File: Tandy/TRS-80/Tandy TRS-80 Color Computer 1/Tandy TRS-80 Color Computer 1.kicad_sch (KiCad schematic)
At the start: 254 parts, among them K1 R7336-1, P1 CARTRIDGE CONNECTOR, P2 DIN-4, P3 DIN-6, P4 DIN-6, P5 DIN-5, Q1 MPS3904, Q2 2N6594, Q3 TIP29, T1 TRANSFORMER, U1 MC6809E, U10 MC6883, U11 74LS138, U12 MC1372, U13 723C, U14 LM339, U15 741C, U16 74LS244, U17 78M12, U18 79M12, U19 79L05, U2 MC14050B, U20 MCM4027A, U21 MCM4027A, U22 MCM4027A, U23 MCM4027A, U24 MCM4027A, U25 MCM4027A, U26 MCM4027A, U27 MCM4027A, U28 MCM68A364, U29 74LS02, U3 MCM68A364, U4 MC6821, U5 UM1285-8 RF Modulator, U6 74LS273, U7 MC6847, U8 MC6821, U9 MC14529B, X1 14.31818MHz

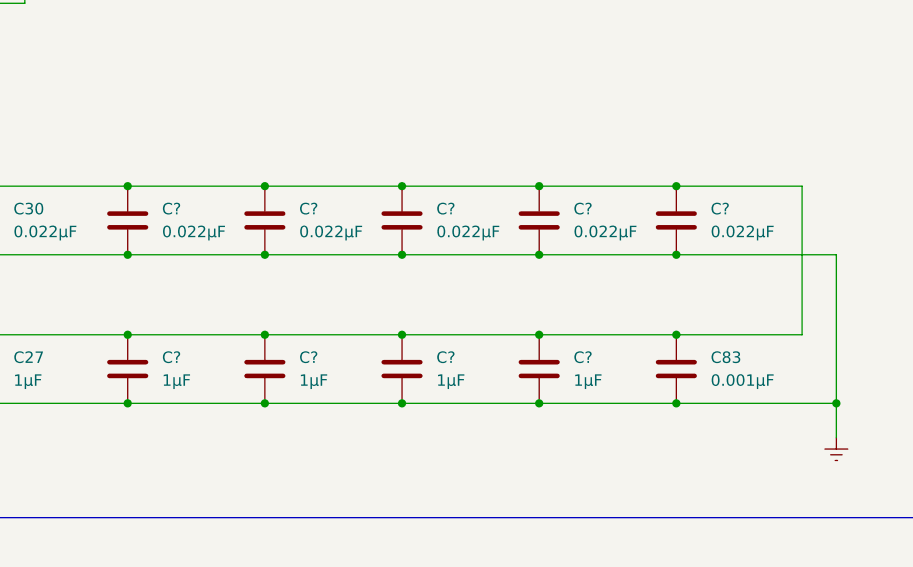
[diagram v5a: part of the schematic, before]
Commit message: Forgot to annotate some caps, fixed!
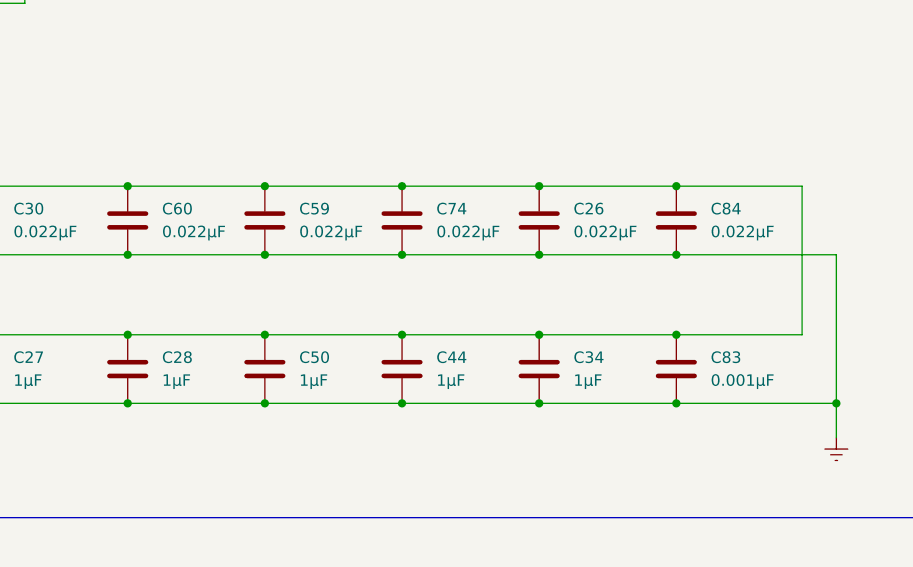
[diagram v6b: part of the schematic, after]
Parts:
- gave numbers to parts that had none: 9
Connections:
- net at E2.: now also T1.; no longer S2.
- net at S2.: now also E1.; no longer CR11. (-)
- net at E1.: now also T1.; no longer S2.
- new net: E2., S2.
- new net: CR11. (-), S2.
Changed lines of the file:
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@@
   (symbol (lib_id "Device:C") (at 646.43 887.73 0) (mirror y) (unit 1)
     (in_bom yes) (on_board yes) (fields_autoplaced)
-    (property "Reference" "C?" (id 0) (at 650.24 886.4599 0)
+    (property "Reference" "C28" (id 0) (at 650.24 886.4599 0)
       (effects (font (size 1.27 1.27)) (justify right))
     )
@@
   (symbol (lib_id "Device:C") (at 661.67 887.73 0) (mirror y) (unit 1)
     (in_bom yes) (on_board yes) (fields_autoplaced)
-    (property "Reference" "C?" (id 0) (at 665.48 886.4599 0)
+    (property "Reference" "C50" (id 0) (at 665.48 886.4599 0)
       (effects (font (size 1.27 1.27)) (justify right))
     )
@@
   (symbol (lib_id "Device:C") (at 646.43 871.22 0) (mirror y) (unit 1)
     (in_bom yes) (on_board yes) (fields_autoplaced)
-    (property "Reference" "C?" (id 0) (at 650.24 869.9499 0)
+    (property "Reference" "C60" (id 0) (at 650.24 869.9499 0)
       (effects (font (size 1.27 1.27)) (justify right))
     )
@@
   (symbol (lib_id "Device:C") (at 692.15 887.73 0) (mirror y) (unit 1)
     (in_bom yes) (on_board yes) (fields_autoplaced)
-    (property "Reference" "C?" (id 0) (at 695.96 886.4599 0)
+    (property "Reference" "C34" (id 0) (at 695.96 886.4599 0)
       (effects (font (size 1.27 1.27)) (justify right))
     )
@@
   (symbol (lib_id "Device:C") (at 676.91 871.22 0) (mirror y) (unit 1)
     (in_bom yes) (on_board yes) (fields_autoplaced)
-    (property "Reference" "C?" (id 0) (at 680.72 869.9499 0)
+    (property "Reference" "C74" (id 0) (at 680.72 869.9499 0)
       (effects (font (size 1.27 1.27)) (justify right))
     )
@@
   (symbol (lib_id "Device:C") (at 707.39 871.22 0) (mirror y) (unit 1)
     (in_bom yes) (on_board yes) (fields_autoplaced)
-    (property "Reference" "C?" (id 0) (at 711.2 869.9499 0)
+    (property "Reference" "C84" (id 0) (at 711.2 869.9499 0)
       (effects (font (size 1.27 1.27)) (justify right))
     )
@@
   (symbol (lib_id "Device:C") (at 676.91 887.73 0) (mirror y) (unit 1)
     (in_bom yes) (on_board yes) (fields_autoplaced)
-    (property "Reference" "C?" (id 0) (at 680.72 886.4599 0)
+    (property "Reference" "C44" (id 0) (at 680.72 886.4599 0)
       (effects (font (size 1.27 1.27)) (justify right))
     )
@@
   (symbol (lib_id "Device:C") (at 692.15 871.22 0) (mirror y) (unit 1)
     (in_bom yes) (on_board yes) (fields_autoplaced)
-    (property "Reference" "C?" (id 0) (at 695.96 869.9499 0)
+    (property "Reference" "C26" (id 0) (at 695.96 869.9499 0)
       (effects (font (size 1.27 1.27)) (justify right))
     )
@@
   (symbol (lib_id "Device:C") (at 661.67 871.22 0) (mirror y) (unit 1)
     (in_bom yes) (on_board yes) (fields_autoplaced)
-    (property "Reference" "C?" (id 0) (at 665.48 869.9499 0)
+    (property "Reference" "C59" (id 0) (at 665.48 869.9499 0)
       (effects (font (size 1.27 1.27)) (justify right))
     )
@@
       (reference "C25") (unit 1) (value "0.1µF") (footprint "")
     )
+    (path "/bf5af0e6-7117-4682-a380-3c04bab5193b"
+      (reference "C26") (unit 1) (value "0.022µF") (footprint "")
+    )
     (path "/b0774126-0c90-4e77-9496-ee04a2f90bf7"
       (reference "C27") (unit 1) (value "1µF") (footprint "")
     )
+    (path "/04f92a1c-8d2a-4a20-87a3-2de5d99d358c"
+      (reference "C28") (unit 1) (value "1µF") (footprint "")
+    )
     (path "/dce6889b-dbc5-438c-b83f-da6b8cc271a5"
       (reference "C29") (unit 1) (value "1µF") (footprint "")
@@
       (reference "C33") (unit 1) (value "1µF") (footprint "")
     )
+    (path "/59425335-7ef7-4358-a16d-e79ce78d8c9b"
+      (reference "C34") (unit 1) (value "1µF") (footprint "")
+    )
     (path "/18852cba-fe96-4822-b067-fe1a9f1e962e"
       (reference "C35") (unit 1) (value "1µF") (footprint "")
@@
       (reference "C43") (unit 1) (value "0.1µF") (footprint "")
     )
+    (path "/b7ed9498-108e-44f3-874f-a97fed71aacc"
+      (reference "C44") (unit 1) (value "1µF") (footprint "")
+    )
     (path "/b0be06e7-7b15-4fde-81ed-b4734ac1ae46"
       (reference "C45") (unit 1) (value "1µF") (footprint "")
@@
       (reference "C49") (unit 1) (value "1µF") (footprint "")
     )
+    (path "/10da64bd-acdd-4437-88c2-59123bbd017c"
+      (reference "C50") (unit 1) (value "1µF") (footprint "")
+    )
     (path "/901cbf07-fee9-4812-9f2a-b89260250a27"
       (reference "C51") (unit 1) (value "39pf") (footprint "")
@@
       (reference "C58") (unit 1) (value "0.01µF") (footprint "")
     )
+    (path "/d90dd9ec-e667-4edb-b617-0933b5d8b0df"
+      (reference "C59") (unit 1) (value "0.022µF") (footprint "")
+    )
+    (path "/128109e8-30f5-49b9-a05c-1800b1379113"
+      (reference "C60") (unit 1) (value "0.022µF") (footprint "")
+    )
     (path "/17ca8796-0090-4935-a9a3-c8939d4876dd"
       (reference "C61") (unit 1) (value "1µF") (footprint "")
@@
       (reference "C73") (unit 1) (value "56pf") (footprint "")
     )
+    (path "/9671dc26-ec91-4e04-a9a2-5e2c0c1f1290"
+      (reference "C74") (unit 1) (value "0.022µF") (footprint "")
+    )
     (path "/6e696e12-029f-4550-90bd-8057ea66aa3d"
       (reference "C75") (unit 1) (value "56pf") (footprint "")
@@
       (reference "C83") (unit 1) (value "0.001µF") (footprint "")
     )
-    (path "/01f58367-cef5-4c0a-a599-b0a033f3ac6e"
-      (reference "C?") (unit 1) (value "0.022µF") (footprint "")
-    )
-    (path "/04f92a1c-8d2a-4a20-87a3-2de5d99d358c"
-      (reference "C?") (unit 1) (value "1µF") (footprint "")
-    )
-    (path "/10da64bd-acdd-4437-88c2-59123bbd017c"
-      (reference "C?") (unit 1) (value "1µF") (footprint "")
-    )
-    (path "/128109e8-30f5-49b9-a05c-1800b1379113"
-      (reference "C?") (unit 1) (value "0.022µF") (footprint "")
-    )
-    (path "/59425335-7ef7-4358-a16d-e79ce78d8c9b"
-      (reference "C?") (unit 1) (value "1µF") (footprint "")
-    )
-    (path "/9671dc26-ec91-4e04-a9a2-5e2c0c1f1290"
-      (reference "C?") (unit 1) (value "0.022µF") (footprint "")
-    )
     (path "/9877a4a1-a062-42e6-8cda-04a919c45af1"
-      (reference "C?") (unit 1) (value "0.022µF") (footprint "")
+      (reference "C84") (unit 1) (value "0.022µF") (footprint "")
     )
-    (path "/b7ed9498-108e-44f3-874f-a97fed71aacc"
-      (reference "C?") (unit 1) (value "1µF") (footprint "")
-    )
-    (path "/bf5af0e6-7117-4682-a380-3c04bab5193b"
-      (reference "C?") (unit 1) (value "0.022µF") (footprint "")
-    )
-    (path "/d90dd9ec-e667-4edb-b617-0933b5d8b0df"
+    (path "/01f58367-cef5-4c0a-a599-b0a033f3ac6e"
       (reference "C?") (unit 1) (value "0.022µF") (footprint "")
     )

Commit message: Rename parts to sort by device, fixed some missing annotations on CoCo1
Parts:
- C2: renamed from C?; value 0.022µF -> 10µF
- CR11: symbol __Retro_Schematics_Library:VM-28 -> __Retro_Schematics_Library:CC1_VM-28
- E1, E2, E3, E4, E5, E6, E7, E8: value Connector -> CC1_Connector; symbol __Retro_Schematics_Library:Connector -> __Retro_Schematics_Library:CC1_Connector
- H51, H53: symbol __Retro_Schematics_Library:UNKNOWN_H_SYMBOL_COCO -> __Retro_Schematics_Library:CC1_UNKNOWN_H_SYMBOL_COCO
- H52-54: renamed from H?; symbol __Retro_Schematics_Library:UNKNOWN_H_SYMBOL_COCO -> __Retro_Schematics_Library:CC1_UNKNOWN_H_SYMBOL_COCO
- K1: symbol __Retro_Schematics_Library:R7336-1 -> __Retro_Schematics_Library:CC1_R7336-1
- KYBD1: symbol __Retro_Schematics_Library:CoCo_1_Keyboard_Matrix -> __Retro_Schematics_Library:CC1_CoCo_1_Keyboard_Matrix
- P2: symbol __Retro_Schematics_Library:DIN-4 -> __Retro_Schematics_Library:CC1_DIN-4
- P3, P4: symbol __Retro_Schematics_Library:DIN-6 -> __Retro_Schematics_Library:CC1_DIN-6
- P5: symbol __Retro_Schematics_Library:DIN-5 -> __Retro_Schematics_Library:CC1_DIN-5
- Q4: renamed from Q?; value PN2222A -> 2N2222
- R20: renamed from R?; value 150Ω -> 360Ω
- R75: symbol __Retro_Schematics_Library:RESISTOR_PAK -> __Retro_Schematics_Library:CC1_RESISTOR_PAK
- S2: symbol __Retro_Schematics_Library:4PTD_SWITCH -> __Retro_Schematics_Library:CC1_4PTD_SWITCH
- T1: symbol __Retro_Schematics_Library:TRFM_COCO1 -> __Retro_Schematics_Library:CC1_TRFM_COCO1
- TP1, TP10, TP11, TP12, TP2, TP3, TP4, TP5, TP9: symbol __Retro_Schematics_Library:Test_Point -> __Retro_Schematics_Library:CC1_Test_Point
- TPX_UNKNOWN: renamed from TP?; value 4K -> ~
- TPX_UNKNOWN: renamed from TPx?; value TestPoint -> ~
- TPX_UNKNOWN: renamed from TPx; value TestPoint -> ~
- U1: symbol __Retro_Schematics_Library:MC6809E -> __Retro_Schematics_Library:CC1_MC6809E
- U10: symbol __Retro_Schematics_Library:MC6883 -> __Retro_Schematics_Library:CC1_MC6883
- U11: symbol __Retro_Schematics_Library:74LS138 -> __Retro_Schematics_Library:CC1_74LS138
- U12: symbol __Retro_Schematics_Library:MC1372 -> __Retro_Schematics_Library:CC1_MC1372
- U13: symbol __Retro_Schematics_Library:723C -> __Retro_Schematics_Library:CC1_723C
- U14: symbol __Retro_Schematics_Library:LM339 -> __Retro_Schematics_Library:CC1_LM339
- U15: symbol __Retro_Schematics_Library:741C -> __Retro_Schematics_Library:CC1_741C
- U16: symbol __Retro_Schematics_Library:74LS244 -> __Retro_Schematics_Library:CC1_74LS244
- U17: symbol __Retro_Schematics_Library:78M12 -> __Retro_Schematics_Library:CC1_78M12
- U18: symbol __Retro_Schematics_Library:79M12 -> __Retro_Schematics_Library:CC1_79M12
- U19: symbol __Retro_Schematics_Library:79L05 -> __Retro_Schematics_Library:CC1_79L05
- U2: symbol __Retro_Schematics_Library:MC14050B -> __Retro_Schematics_Library:CC1_MC14050B
- U20, U21, U22, U23, U24, U25, U26, U27: symbol __Retro_Schematics_Library:MCM4027A -> __Retro_Schematics_Library:CC1_MCM4027A
- U28, U3: symbol __Retro_Schematics_Library:MCM68A364 -> __Retro_Schematics_Library:CC1_MCM68A364
- U29: symbol __Retro_Schematics_Library:74LS02 -> __Retro_Schematics_Library:CC1_74LS02
- U4, U8: symbol __Retro_Schematics_Library:MC6821 -> __Retro_Schematics_Library:CC1_MC6821
- U5: symbol __Retro_Schematics_Library:UM1285-8 RF Modulator -> __Retro_Schematics_Library:CC1_UM1285-8 RF Modulator
- U6: symbol __Retro_Schematics_Library:74LS273 -> __Retro_Schematics_Library:CC1_74LS273
- U7: symbol __Retro_Schematics_Library:MC6847 -> __Retro_Schematics_Library:CC1_MC6847
- U9: symbol __Retro_Schematics_Library:MC14529B -> __Retro_Schematics_Library:CC1_MC14529B
- gave numbers to parts that had none: 1
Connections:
- net at E2.: now also T1.; no longer S2.
- net at S2.: now also E1.; no longer CR11. (-)
- net at E1.: now also T1.; no longer S2.
- new net: E2., S2.
- new net: CR11. (-), S2.

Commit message: Modified TRS80 CoCo 1 library from global to local and removed global library.
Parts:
- CR11: symbol __Retro_Schematics_Library:CC1_VM-28 -> Tandy_TRS80_CoCo_1:CC1_VM-28
- E1, E2, E3, E4, E5, E6, E7, E8: symbol __Retro_Schematics_Library:CC1_Connector -> Tandy_TRS80_CoCo_1:CC1_Connector
- H51, H52-54, H53: symbol __Retro_Schematics_Library:CC1_UNKNOWN_H_SYMBOL_COCO -> Tandy_TRS80_CoCo_1:CC1_UNKNOWN_H_SYMBOL_COCO
- K1: symbol __Retro_Schematics_Library:CC1_R7336-1 -> Tandy_TRS80_CoCo_1:CC1_R7336-1
- KYBD1: symbol __Retro_Schematics_Library:CC1_CoCo_1_Keyboard_Matrix -> Tandy_TRS80_CoCo_1:CC1_CoCo_1_Keyboard_Matrix
- P2: symbol __Retro_Schematics_Library:CC1_DIN-4 -> Tandy_TRS80_CoCo_1:CC1_DIN-4
- P3, P4: symbol __Retro_Schematics_Library:CC1_DIN-6 -> Tandy_TRS80_CoCo_1:CC1_DIN-6
- P5: symbol __Retro_Schematics_Library:CC1_DIN-5 -> Tandy_TRS80_CoCo_1:CC1_DIN-5
- R75: symbol __Retro_Schematics_Library:CC1_RESISTOR_PAK -> Tandy_TRS80_CoCo_1:CC1_RESISTOR_PAK
- S2: symbol __Retro_Schematics_Library:CC1_4PTD_SWITCH -> Tandy_TRS80_CoCo_1:CC1_4PTD_SWITCH
- T1: symbol __Retro_Schematics_Library:CC1_TRFM_COCO1 -> Tandy_TRS80_CoCo_1:CC1_TRFM_COCO1
- TP1, TP10, TP11, TP12, TP2, TP3, TP4, TP5, TP9: symbol __Retro_Schematics_Library:CC1_Test_Point -> Tandy_TRS80_CoCo_1:CC1_Test_Point
- U1: symbol __Retro_Schematics_Library:CC1_MC6809E -> Tandy_TRS80_CoCo_1:CC1_MC6809E
- U10: symbol __Retro_Schematics_Library:CC1_MC6883 -> Tandy_TRS80_CoCo_1:CC1_MC6883
- U11: symbol __Retro_Schematics_Library:CC1_74LS138 -> Tandy_TRS80_CoCo_1:CC1_74LS138
- U12: symbol __Retro_Schematics_Library:CC1_MC1372 -> Tandy_TRS80_CoCo_1:CC1_MC1372
- U13: symbol __Retro_Schematics_Library:CC1_723C -> Tandy_TRS80_CoCo_1:CC1_723C
- U14: symbol __Retro_Schematics_Library:CC1_LM339 -> Tandy_TRS80_CoCo_1:CC1_LM339
- U15: symbol __Retro_Schematics_Library:CC1_741C -> Tandy_TRS80_CoCo_1:CC1_741C
- U16: symbol __Retro_Schematics_Library:CC1_74LS244 -> Tandy_TRS80_CoCo_1:CC1_74LS244
- U17: symbol __Retro_Schematics_Library:CC1_78M12 -> Tandy_TRS80_CoCo_1:CC1_78M12
- U18: symbol __Retro_Schematics_Library:CC1_79M12 -> Tandy_TRS80_CoCo_1:CC1_79M12
- U19: symbol __Retro_Schematics_Library:CC1_79L05 -> Tandy_TRS80_CoCo_1:CC1_79L05
- U2: symbol __Retro_Schematics_Library:CC1_MC14050B -> Tandy_TRS80_CoCo_1:CC1_MC14050B
- U20, U21, U22, U23, U24, U25, U26, U27: symbol __Retro_Schematics_Library:CC1_MCM4027A -> Tandy_TRS80_CoCo_1:CC1_MCM4027A
- U28, U3: symbol __Retro_Schematics_Library:CC1_MCM68A364 -> Tandy_TRS80_CoCo_1:CC1_MCM68A364
- U29: symbol __Retro_Schematics_Library:CC1_74LS02 -> Tandy_TRS80_CoCo_1:CC1_74LS02
- U4, U8: symbol __Retro_Schematics_Library:CC1_MC6821 -> Tandy_TRS80_CoCo_1:CC1_MC6821
- U5: symbol __Retro_Schematics_Library:CC1_UM1285-8 RF Modulator -> Tandy_TRS80_CoCo_1:CC1_UM1285-8 RF Modulator
- U6: symbol __Retro_Schematics_Library:CC1_74LS273 -> Tandy_TRS80_CoCo_1:CC1_74LS273
- U7: symbol __Retro_Schematics_Library:CC1_MC6847 -> Tandy_TRS80_CoCo_1:CC1_MC6847
- U9: symbol __Retro_Schematics_Library:CC1_MC14529B -> Tandy_TRS80_CoCo_1:CC1_MC14529B
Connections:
- net at E2.: now also T1.; no longer S2.
- net at S2.: now also E1.; no longer CR11. (-)
- net at E1.: now also T1.; no longer S2.
- new net: E2., S2.
- new net: CR11. (-), S2.
